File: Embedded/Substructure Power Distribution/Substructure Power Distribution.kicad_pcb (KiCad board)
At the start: 4 copper layers, 55 x 20 mm, 66 parts, among them J1 S JST, J2 D0 FFC, J3 D1 FFC, J4 S Pins A, J5 S Pins B, Q1 CSD17577Q5A, Q2 CSD17577Q5A, Q3 CSD17573Q5B, Q4 CSD17577Q5A, U1 LM5176PWP, U2 INA220AIDGSR, U3 SI7111EDN-T1-GE3, U4 SI7111EDN-T1-GE3, U5 TN5015H-6G-TR

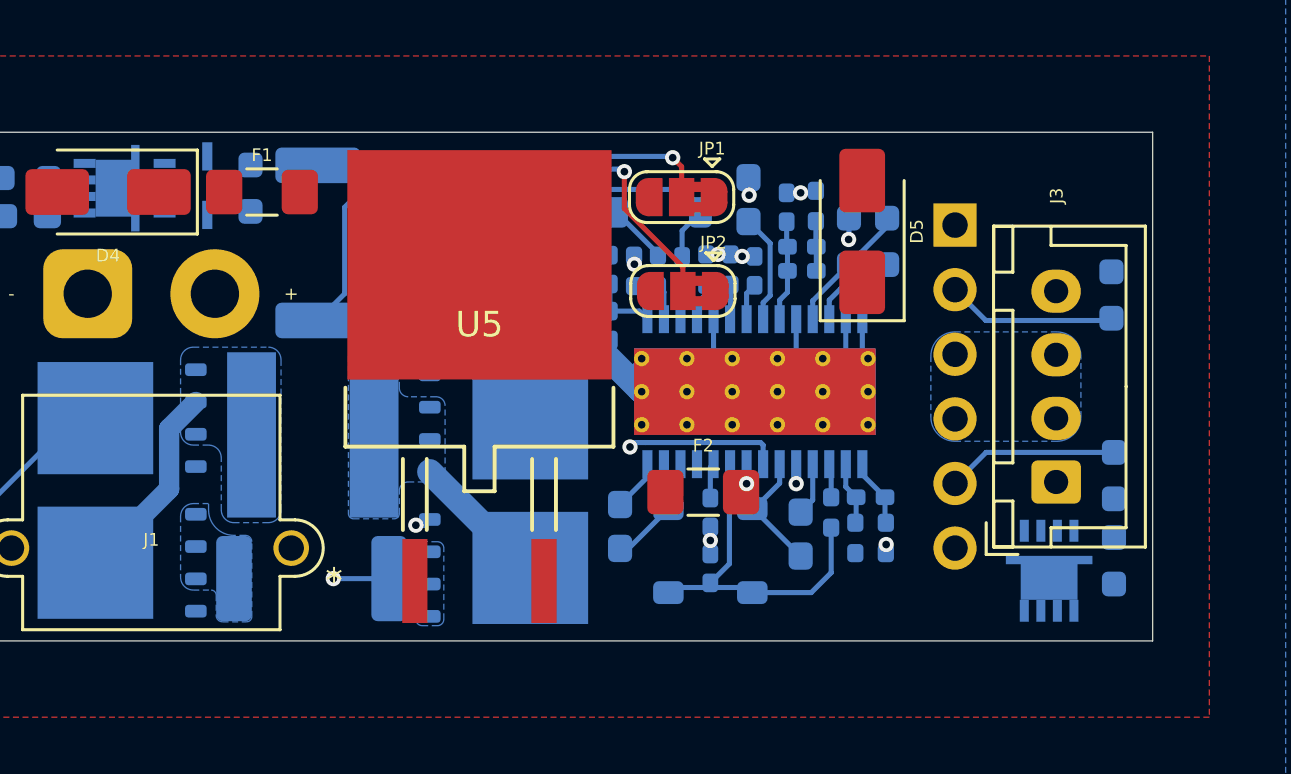
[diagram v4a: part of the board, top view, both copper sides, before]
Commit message: Added 5V Only PSU
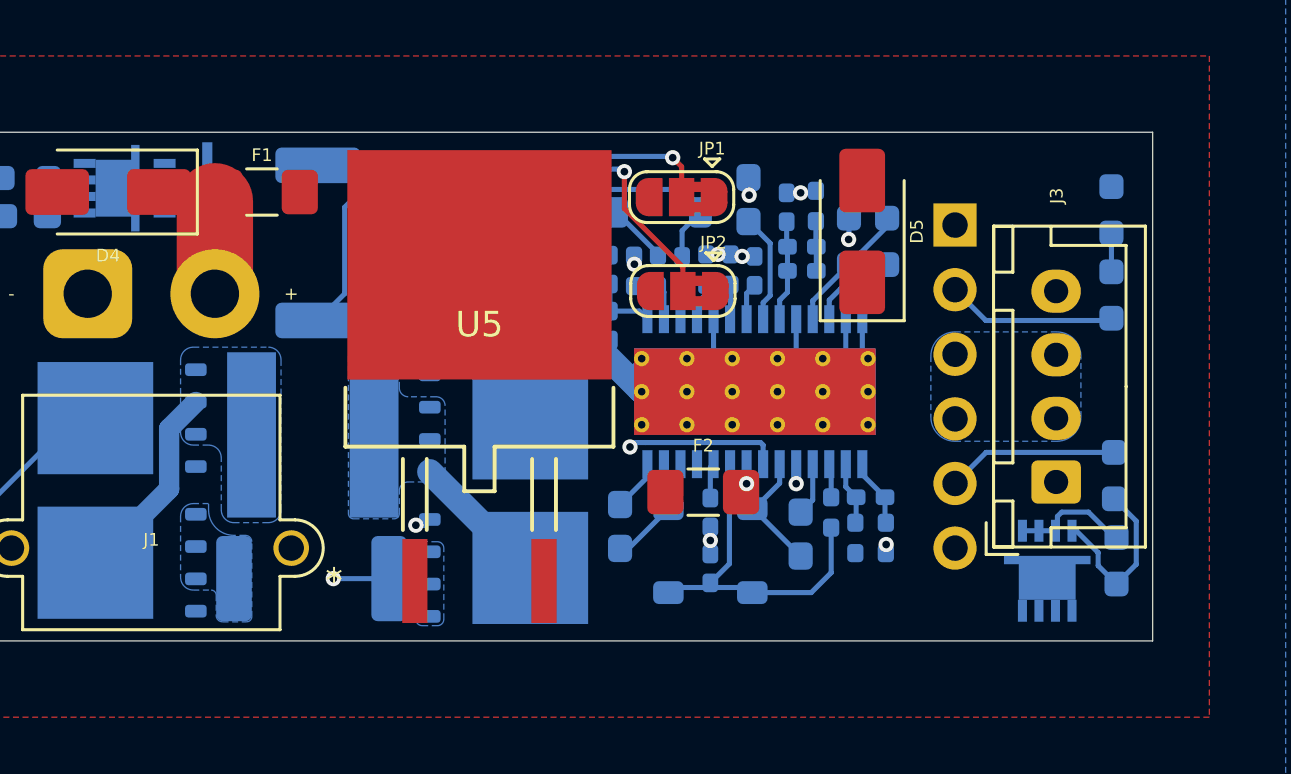
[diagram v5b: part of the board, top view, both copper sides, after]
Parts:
- moved R17 33.9 mm to (126.2, 108.0)
- moved R19 0.10 mm to (126.3, 121.8)
- moved U4 0.08 mm to (123.6, 122.2)
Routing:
- net Net-(U4-G): track 0.00 -> 7.00 mm
- net +RAWVS: track 0.00 -> 6.71 mm
- net +5V: track 0.00 -> 4.57 mm
- net Net-(U3-G): track 0.00 -> 1.52 mm
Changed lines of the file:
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@@
 	(footprint "Resistor_SMD:R_0603_1608Metric_Pad0.98x0.95mm_HandSolder"
 		(layer "B.Cu")
-		(at 92.3 107.2 90)
+		(at 126.15 108.05 90)
 		(descr "Resistor SMD 0603 (1608 Metric), square (rectangular) end terminal, IPC-7351 nominal with elongated pad for handsoldering. (Body size source: IPC-SM-782 page 72, https://www.pcb-3d.com/wordpress/wp-content/uploads/ipc-sm-782a_amendment_1_and_2.pdf), generated with kicad-footprint-generator")
 		(tags "resistor handsolder")
@@
 	(footprint "P Channel Mosfet:MOSFET_0DN-T1-GE3_VIS"
 		(layer "B.Cu")
-		(at 123.7 122.2414 90)
+		(at 123.624999 122.2414 90)
 		(tags "SI7111EDN-T1-GE3 ")
 		(property "Reference" "U4"
@@
 	(footprint "Resistor_SMD:R_0603_1608Metric_Pad0.98x0.95mm_HandSolder"
 		(layer "B.Cu")
-		(at 126.25 121.85 -90)
+		(at 126.35 121.85 -90)
 		(descr "Resistor SMD 0603 (1608 Metric), square (rectangular) end terminal, IPC-7351 nominal with elongated pad for handsoldering. (Body size source: IPC-SM-782 page 72, https://www.pcb-3d.com/wordpress/wp-content/uploads/ipc-sm-782a_amendment_1_and_2.pdf), generated with kicad-footprint-generator")
 		(tags "resistor handsolder")
@@
 	)
 	(segment
+		(start 125.248101 119.935601)
+		(end 126.25 120.9375)
+		(width 0.2)
+		(layer "B.Cu")
+		(net 11)
+	)
+	(segment
+		(start 124.025001 120.668401)
+		(end 124.025001 120.106799)
+		(width 0.2)
+		(layer "B.Cu")
+		(net 11)
+	)
+	(segment
+		(start 122.725001 120.668401)
+		(end 124.025001 120.668401)
+		(width 0.2)
+		(layer "B.Cu")
+		(net 11)
+	)
+	(segment
+		(start 124.025001 120.106799)
+		(end 124.196199 119.935601)
+		(width 0.2)
+		(layer "B.Cu")
+		(net 11)
+	)
+	(segment
+		(start 124.196199 119.935601)
+		(end 125.248101 119.935601)
+		(width 0.2)
+		(layer "B.Cu")
+		(net 11)
+	)
+	(segment
 		(start 106.83 121.3625)
 		(end 107.1675 121.3625)
@@
 	)
 	(segment
+		(start 90.9 111.35)
+		(end 90.9 107.7125)
+		(width 3)
+		(layer "F.Cu")
+		(net 21)
+	)
+	(segment
+		(start 90.9 107.7125)
+		(end 91.2625 107.35)
+		(width 0.2)
+		(layer "F.Cu")
+		(net 21)
+	)
+	(segment
+		(start 91.2625 107.35)
+		(end 88.7 107.35)
+		(width 0.5)
+		(layer "F.Cu")
+		(net 21)
+	)
+	(segment
 		(start 121.2225 117.5875)
 		(end 126.25 117.5875)
@@
 		(net 40)
 	)
+	(segment
+		(start 126.15 108.9625)
+		(end 126.15 110.4875)
+		(width 0.2)
+		(layer "B.Cu")
+		(net 42)
+	)
+	(segment
+		(start 124.765481 120.668401)
+		(end 125.627799 121.530719)
+		(width 0.2)
+		(layer "B.Cu")
+		(net 44)
+	)
+	(segment
+		(start 124.599998 120.668401)
+		(end 124.765481 120.668401)
+		(width 0.2)
+		(layer "B.Cu")
+		(net 44)
+	)
+	(segment
+		(start 127.126 120.2885)
+		(end 126.25 119.4125)
+		(width 0.2)
+		(layer "B.Cu")
+		(net 44)
+	)
+	(segment
+		(start 126.35 122.7625)
+		(end 127.126 121.9865)
+		(width 0.2)
+		(layer "B.Cu")
+		(net 44)
+	)
+	(segment
+		(start 127.126 121.9865)
+		(end 127.126 120.2885)
+		(width 0.2)
+		(layer "B.Cu")
+		(net 44)
+	)
+	(segment
+		(start 126.35 122.7625)
+		(end 126.4 122.7625)
+		(width 0.2)
+		(layer "B.Cu")
+		(net 44)
+	)
+	(segment
+		(start 125.627799 121.530719)
+		(end 125.627799 122.040299)
+		(width 0.2)
+		(layer "B.Cu")
+		(net 44)
+	)
+	(segment
+		(start 125.627799 122.040299)
+		(end 126.35 122.7625)
+		(width 0.2)
+		(layer "B.Cu")
+		(net 44)
+	)
 	(zone
 		(net 0)
@@
 		(min_thickness 0.25)
 		(filled_areas_thickness no)
-		(fill yes
+		(fill
 			(thermal_gap 0.5)
 			(thermal_bridge_width 0.5)
@@
 		(min_thickness 0.25)
 		(filled_areas_thickness no)
-		(fill yes
+		(fill
 			(thermal_gap 0.5)
 			(thermal_bridge_width 0.5)
@@
 		(min_thickness 0.25)
 		(filled_areas_thickness no)
-		(fill yes
+		(fill
 			(thermal_gap 0.5)
 			(thermal_bridge_width 0.5)
@@
 		(min_thickness 0.25)
 		(filled_areas_thickness no)
-		(fill yes
+		(fill
 			(thermal_gap 0.5)
 			(thermal_bridge_width 0.5)
@@
 		(min_thickness 0.25)
 		(filled_areas_thickness no)
-		(fill yes
+		(fill
 			(thermal_gap 0.5)
 			(thermal_bridge_width 0.5)
@@
 		(min_thickness 0.25)
 		(filled_areas_thickness no)
-		(fill yes
+		(fill
 			(thermal_gap 0.5)
 			(thermal_bridge_width 0.5)
@@
 		(min_thickness 0.25)
 		(filled_areas_thickness no)
-		(fill yes
+		(fill
 			(thermal_gap 0.5)
 			(thermal_bridge_width 0.5)
@@
 		(min_thickness 0.25)
 		(filled_areas_thickness no)
-		(fill yes
+		(fill
 			(thermal_gap 0.5)
 			(thermal_bridge_width 0.5)
@@
 		(min_thickness 0.25)
 		(filled_areas_thickness no)
-		(fill yes
+		(fill
 			(thermal_gap 0.5)
 			(thermal_bridge_width 0.5)
@@
 		(min_thickness 0.25)
 		(filled_areas_thickness no)
-		(fill yes
+		(fill
 			(thermal_gap 0.5)
 			(thermal_bridge_width 0.5)
